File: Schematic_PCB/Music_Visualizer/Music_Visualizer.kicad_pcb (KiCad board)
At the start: 2 copper layers, 141.5 x 82 mm, 264 parts, among them J3 Screw_Terminal_01x02, J5 Screw_Terminal_01x02, J6 3.5mm, Q1 DMP2123LQ-7, SW1 SW_Slide_DPDT, SW2 SW_SPST, U1 LM324, U10 LM3915N-1, U11 LM3915N-1, U12 LM3915N-1, U13 LM3915N-1, U14 LM3915N-1, U15 LM3915N-1, U16 LM3915N-1, U2 LM324, U3 LM324, U4 LM324, U5 LM324, U6 LM324, U7 LM324, U8 LM324

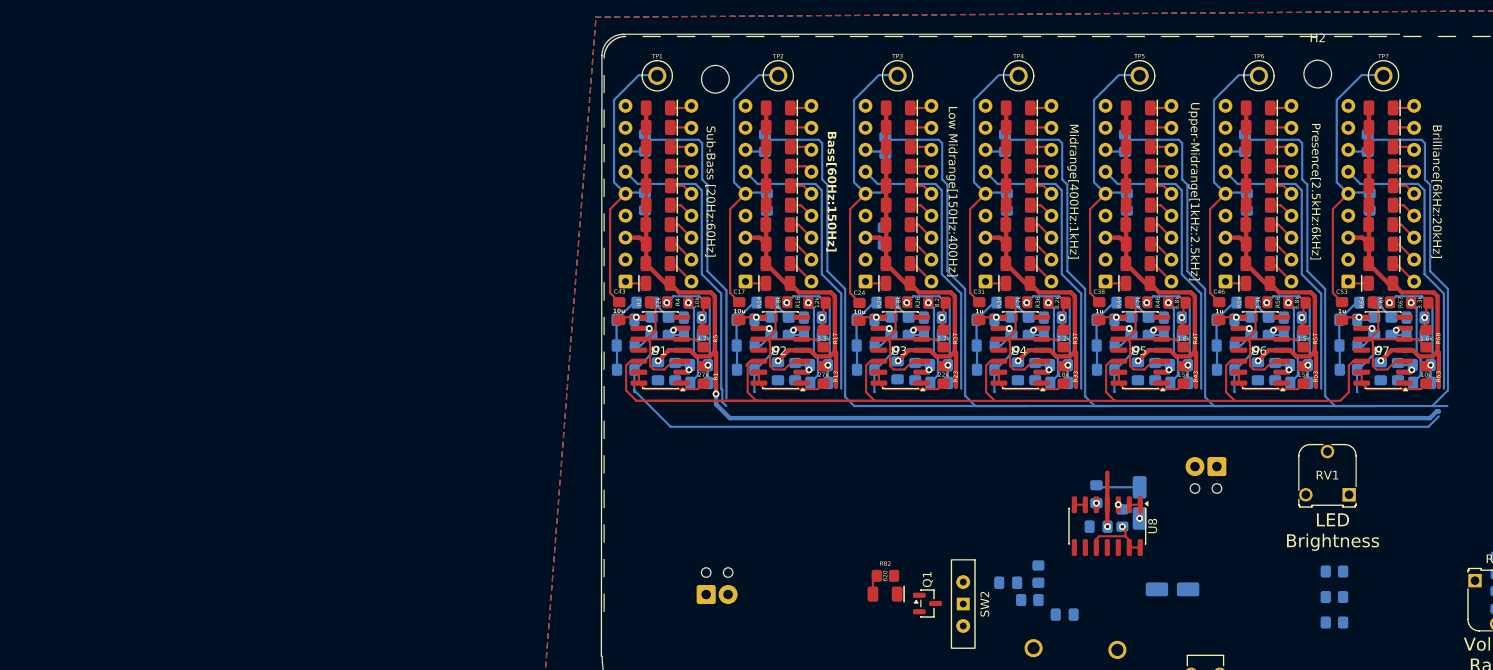
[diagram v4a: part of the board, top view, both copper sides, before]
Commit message: Refine traces layout
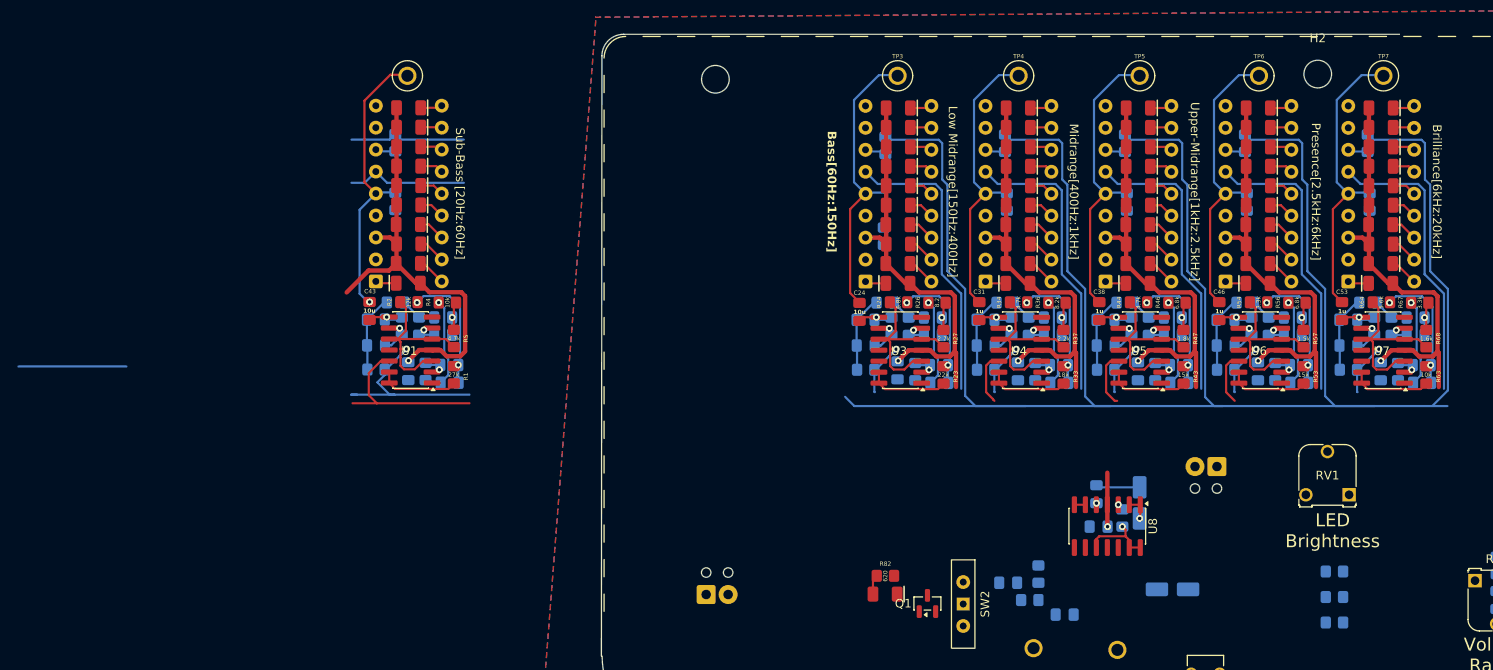
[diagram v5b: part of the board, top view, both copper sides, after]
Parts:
- removed C11, C12, C13, C14, C15, C16, C60: 100n, Custom_Footprints:custom_C_0805_2012Metric_Pad1.18x1.45mm_HandSolder
- removed C17: 10u, Custom_Footprints:custom_C_0805_2012Metric_Pad1.18x1.45mm_HandSolder
- removed D11, D12, D13, D14, D15, D16, D17: LED, PCM_SparkFun-LED:LED_1206_3216Metric_Green
- removed D18, D19: LED, PCM_SparkFun-LED:LED_1206_3216Metric_Yellow
- removed D20: LED, PCM_SparkFun-LED:LED_1206_3216Metric_Red
- removed R13: 27k, Custom_Footprints:R_0805_2012Metric_Pad1.20x1.40mm_HandSolder
- removed R14: 6.8k, Custom_Footprints:R_0805_2012Metric_Pad1.20x1.40mm_HandSolder
- removed R15: 120k, Custom_Footprints:R_0805_2012Metric_Pad1.20x1.40mm_HandSolder
- removed R16: 12k, Custom_Footprints:R_0805_2012Metric_Pad1.20x1.40mm_HandSolder
- removed R17: 3.3k, Custom_Footprints:R_0805_2012Metric_Pad1.20x1.40mm_HandSolder
- removed R18: 56k, Custom_Footprints:R_0805_2012Metric_Pad1.20x1.40mm_HandSolder
- removed R19: 18k, Custom_Footprints:R_0805_2012Metric_Pad1.20x1.40mm_HandSolder
- removed R20: 15k, Custom_Footprints:R_0805_2012Metric_Pad1.20x1.40mm_HandSolder
- removed R21: 39k, Custom_Footprints:R_0805_2012Metric_Pad1.20x1.40mm_HandSolder
- removed R22: 1k, Custom_Footprints:R_0805_2012Metric_Pad1.20x1.40mm_HandSolder
- removed R76: 680, Custom_Footprints:R_0805_2012Metric_Pad1.20x1.40mm_HandSolder
- removed TP2: T_B, Custom_Footprints:TEST1Y
- removed U11: LM3915N-1, Package_DIP:DIP-18_W7.62mm
- removed U2: LM324, Package_SO:SOIC-14_3.9x8.7mm_P1.27mm
- moved TP1 28.9 mm to (-10.4, 16.9)
- moved C1 28.9 mm to (-5.54, 52.4)
- moved C3 28.9 mm to (-6.29, 44.8)
- moved C4 28.9 mm to (-6.29, 46.8)
- moved C43 28.9 mm to (-14.8, 44.1)
- moved C2 28.9 mm to (-5.58, 50.3)
- moved C5 28.9 mm to (-14.1, 45.1)
- moved C59 28.9 mm to (-10.3, 51.0)
- moved C6 28.9 mm to (-14.1, 48.1)
- moved D1 28.9 mm to (-10.3, 40.9)
- moved D10 28.9 mm to (-10.3, 20.6)
- moved D2 28.9 mm to (-10.3, 38.6)
- moved D3 28.9 mm to (-10.3, 36.3)
- moved D4 28.9 mm to (-10.3, 34.1)
- moved D5 28.9 mm to (-10.3, 31.8)
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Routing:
- net +9V: track 432.7 -> 300.3 mm, vias 9 -> 7
- net VCC4_5: track 321.0 -> 210.8 mm, vias 8 -> 7
- net Vsig: track 159.6 -> 56.8 mm
- net LED_Brightness_Control: track 353.9 -> 292.2 mm
- net Rhi_Value: track 237.4 -> 182.1 mm
- net VBass: track 33.7 -> 0.00 mm
- net Net-(C11-Pad1): track 14.7 -> 0.00 mm, vias 2 -> 0
- net Net-(C11-Pad2): track 10.1 -> 0.00 mm, vias 1 -> 0
- net Net-(U2D--): track 9.29 -> 0.00 mm
- net Net-(C15-Pad1): track 9.27 -> 0.00 mm
- net Net-(C13-Pad1): track 5.25 -> 0.00 mm, vias 1 -> 0
- net Net-(U2C--): track 4.51 -> 0.00 mm, vias 1 -> 0
- net Net-(C15-Pad2): track 4.48 -> 0.00 mm, vias 1 -> 0
- net Net-(D12-K): track 3.33 -> 0.00 mm
- net Net-(D13-K): track 3.17 -> 0.00 mm
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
